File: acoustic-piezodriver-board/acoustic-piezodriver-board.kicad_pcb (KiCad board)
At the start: 4 copper layers, 86 x 90 mm, 129 parts, among them J301 Conn_02x06_Odd_Even, J501 Conn_02x06_Odd_Even, P201 WJ128V-5.0-3P, P301 WJ128V-5.0-3P, Q501 AO3400A, Q502 AO3400A, U10 NCE6005AS, U201 UCC27282DR, U202 UCC27282DR, U401 AMS1117-3.3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

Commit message: finished schematic, routing
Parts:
- removed P301: WJ128V-5.0-3P, iw-connector:WJ128V-5.0-3P
- removed U401: AMS1117-3.3, Package_TO_SOT_SMD:SOT-223-3_TabPin2
- added C101: 22uF, Capacitor_SMD:C_0805_2012Metric, F.Cu at (-48.2, 146.8)
- added C102: 0.1uF, Capacitor_SMD:C_0402_1005Metric, F.Cu at (-42.0, 128.7)
- added C103: 1nF, Capacitor_SMD:C_0402_1005Metric, F.Cu at (-42.0, 130.7)
- added C210: 0.1uF, Capacitor_SMD:C_0402_1005Metric, F.Cu at (-37.1, 134.7)
- added C211: 1nF, Capacitor_SMD:C_0402_1005Metric, F.Cu at (-37.1, 136.7)
- added C301: 0.1uF, Capacitor_SMD:C_0201_0603Metric, F.Cu at (-38.9, 159.2)
- added C304: 0.1uF, Capacitor_SMD:C_0402_1005Metric, F.Cu at (-38.7, 157.3)
- added C404: 0.1uF, Capacitor_SMD:C_0402_1005Metric, F.Cu at (-51.9, 153.3)
- added C405: 220nF, Capacitor_SMD:C_0402_1005Metric, F.Cu at (-51.9, 155.2)
- added C406: 220nF, Capacitor_SMD:C_0402_1005Metric, F.Cu at (-51.9, 157.2)
- added C523: 0.1uF, Capacitor_SMD:C_0402_1005Metric, F.Cu at (-33.1, 140.7)
- added C524: 0.1uF, Capacitor_SMD:C_0402_1005Metric, F.Cu at (-33.1, 142.6)
- added L301: 100uH, iw-inductor:PSPMAA1050H-101M-ANP, F.Cu at (108.2, 120.4)
- added L501: 100uH, iw-inductor:PSPMAA1050H-101M-ANP, F.Cu at (-48.1, 178.0)
- added L502: 100uH, iw-inductor:PSPMAA1050H-101M-ANP, F.Cu at (-48.1, 189.3)
- added P101: WJ128V-5.0-3P, iw-connector:WJ128V-5.0-3P, F.Cu at (-51.6, 133.3)
- added R406: 0, Resistor_SMD:R_0603_1608Metric_Pad0.98x0.95mm_HandSolder, F.Cu at (-48.3, 154.1)
- added R407: 10k, Resistor_SMD:R_0603_1608Metric, F.Cu at (-58.3, 151.6)
- added R408: 10k, Resistor_SMD:R_0603_1608Metric, F.Cu at (-58.3, 154.1)
- added R409: 1k, Resistor_SMD:R_0402_1005Metric, F.Cu at (-54.8, 151.3)
- added R410: 1k, Resistor_SMD:R_0402_1005Metric, F.Cu at (-54.8, 153.3)
- added R411: 10k, Resistor_SMD:R_0603_1608Metric, F.Cu at (-58.3, 156.6)
- added R412: 1k8, Resistor_SMD:R_0603_1608Metric, F.Cu at (-58.3, 159.1)
- added R413: 20k, Resistor_SMD:R_0402_1005Metric, F.Cu at (-54.8, 155.3)
- added R414: 1k, Resistor_SMD:R_0402_1005Metric, F.Cu at (-54.8, 157.3)
- added TP301: TestPoint_Flag, TestPoint:TestPoint_THTPad_D2.0mm_Drill1.0mm, F.Cu at (-42.1, 158.4)
- added TP501: TestPoint_Flag, TestPoint:TestPoint_THTPad_D2.0mm_Drill1.0mm, F.Cu at (-36.6, 141.7)
- added TP502: TestPoint_Flag, TestPoint:TestPoint_THTPad_D2.0mm_Drill1.0mm, F.Cu at (-36.6, 145.8)
- added U101: AMS1117-3.3, Package_TO_SOT_SMD:SOT-223-3_TabPin2, F.Cu at (-55.4, 143.5)
- added U102: TMCS1108A3UQDR, iw-power:TMCS1108A3UQDR, F.Cu at (-45.6, 142.3)
- added U204: TMCS1108A3UQDR, iw-power:TMCS1108A3UQDR, F.Cu at (-33.7, 130.7)
- added U302: TMCS1108A3UQDR, iw-power:TMCS1108A3UQDR, F.Cu at (-39.3, 153.3)
- added U404: ADS1115IDGS, Package_SO:TSSOP-10_3x3mm_P0.5mm, F.Cu at (-49.9, 160.5)
- C402: value 22uF -> 220nF; footprint Capacitor_SMD:C_0805_2012Metric -> Capacitor_SMD:C_0402_1005Metric
- L4: footprint iw-inductor:PSPMAC1045H-101M-ANP -> iw-inductor:PSPMAA1050H-101M-ANP
- R402: value 4.7k -> 0; footprint Resistor_SMD:R_0402_1005Metric -> Resistor_SMD:R_0603_1608Metric_Pad0.98x0.95mm_HandSolder
- moved R402 73.2 mm to (-48.3, 151.6)
- moved C402 64.7 mm to (-51.9, 151.3)
- moved C8 21.0 mm to (65.1, 90.2)
- moved R5 21.0 mm to (65.2, 96.4)
- moved C2 21.0 mm to (51.1, 117.2)
- moved C3 21.0 mm to (48.9, 83.0)
- moved C4 21.0 mm to (38.9, 112.5)
- moved C9 21.0 mm to (44.8, 105.0)
- moved D11 21.0 mm to (54.6, 113.9)
- moved D9 21.0 mm to (45.8, 111.2)
- moved R1 21.0 mm to (51.7, 113.9)
- moved R2 21.0 mm to (62.7, 111.1)
- moved R4 21.0 mm to (42.9, 111.0)
- moved U201 21.0 mm to (60.2, 116.2)
- moved U202 21.0 mm to (40.2, 116.3)
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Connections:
- C3 pad 1: /INVERTER/VDC -> /INVERTER/VINV_N
- C4 pad 1: /INVERTER/VDC -> /INVERTER/VINV_N
- C40 pad 1: /COMPUTE_POWER/6V -> +6V
- C402 pad 1: +3V3 -> Net-(U404-AIN1)
- C41 pad 1: /COMPUTE_POWER/6V -> +6V
- C42 pad 1: /COMPUTE_POWER/6V -> +6V
- C43 pad 1: /COMPUTE_POWER/6V -> +6V
- C516 pad 1: /INVERTER/VDC -> /INVERTER/VINV_P
- C517 pad 1: /INVERTER/VDC -> /INVERTER/VINV_P
- C518 pad 1: /INVERTER/VDC -> /INVERTER/VINV_P
- C519 pad 1: /INVERTER/VDC -> /INVERTER/VINV_P
- D2 pad 1: /COMPUTE_POWER/6V -> +6V
- D501 pad 1: /INVERTER/VDC -> /INVERTER/VINV_P
- D504 pad 1: /INVERTER/VDC -> /INVERTER/VINV_P
- J301 pad 10: /COMPUTE_POWER/6V -> /COMPUTE_POWER/6V_N
- J301 pad 12: /COMPUTE_POWER/6V -> /COMPUTE_POWER/6V_N
- J301 pad 2: /COMPUTE_POWER/6V -> /COMPUTE_POWER/6V_N
- J301 pad 4: /COMPUTE_POWER/6V -> /COMPUTE_POWER/6V_N
- J301 pad 6: /COMPUTE_POWER/6V -> /COMPUTE_POWER/6V_N
- J301 pad 8: /COMPUTE_POWER/6V -> /COMPUTE_POWER/6V_N
- J501 pad 5: unconnected-(J501-Pin_5-Pad5) -> /SENSORS_CONN/ADC_ALERT
- R10 pad 2: /INVERTER/VDC -> /INVERTER/VINV_N
- R23 pad 1: /COMPUTE_POWER/6V -> +6V
- R512 pad 1: /INVERTER/VDC -> /INVERTER/VINV_P
- R7 pad 2: /INVERTER/VDC -> /INVERTER/VINV_N
- U201 pad 1: /INVERTER/VDC -> /INVERTER/VINV_N
- U202 pad 1: /INVERTER/VDC -> /INVERTER/VINV_N
- U403 pad 4: GND -> Net-(U403-ADD0)
- U6 pad 7: /INVERTER/VDC -> /INVERTER/VINV_N
- U6 pad 8: /INVERTER/VDC -> /INVERTER/VINV_N
- U7 pad 7: /INVERTER/VDC -> /INVERTER/VINV_N
- U7 pad 8: /INVERTER/VDC -> /INVERTER/VINV_N

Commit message: replaced dual 10uH inductors with single 22uH higher VDC resistant one, started laying out 40 V boost
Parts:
- removed C103, C211: 1nF, Capacitor_SMD:C_0402_1005Metric
- removed L4: 100uH, iw-inductor:PSPMAA1050H-101M-ANP
- removed TP301: TestPoint_Flag, TestPoint:TestPoint_THTPad_D2.0mm_Drill1.0mm
- added L302: 100uH, iw-inductor:PSPMAA1050H-101M-ANP, F.Cu at (123.0, 124.5)
- added L505: 22uH, iw-inductor:PA4343.223NLT, F.Cu at (69.3, 61.5)
- moved C501 207.7 mm to (75.9, 162.5)
- moved C503 207.7 mm to (58.3, 162.4)
- moved C505 207.7 mm to (58.3, 165.4)
- moved C506 207.7 mm to (58.3, 168.4)
- moved C507 207.7 mm to (58.3, 171.4)
- moved C508 207.7 mm to (58.3, 174.4)
- moved C510 207.7 mm to (80.2, 161.8)
- moved C511 207.7 mm to (80.2, 163.8)
- moved D503 207.7 mm to (69.1, 167.7)
- moved U502 207.7 mm to (76.8, 173.3)
- moved R505 203.0 mm to (91.8, 174.0)
- moved Q501 200.6 mm to (78.3, 177.3)
- moved U501 200.6 mm to (69.5, 178.0)
- moved C512 200.2 mm to (53.9, 178.2)
- moved R506 200.2 mm to (57.9, 178.2)
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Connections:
- U102 pad 6: unconnected-(U102-NC-Pad6) -> GND
- U201 pad 9: (no net) -> GND
- U202 pad 9: (no net) -> GND
- U204 pad 6: unconnected-(U204-NC-Pad6) -> GND
- U302 pad 6: unconnected-(U302-NC-Pad6) -> GND

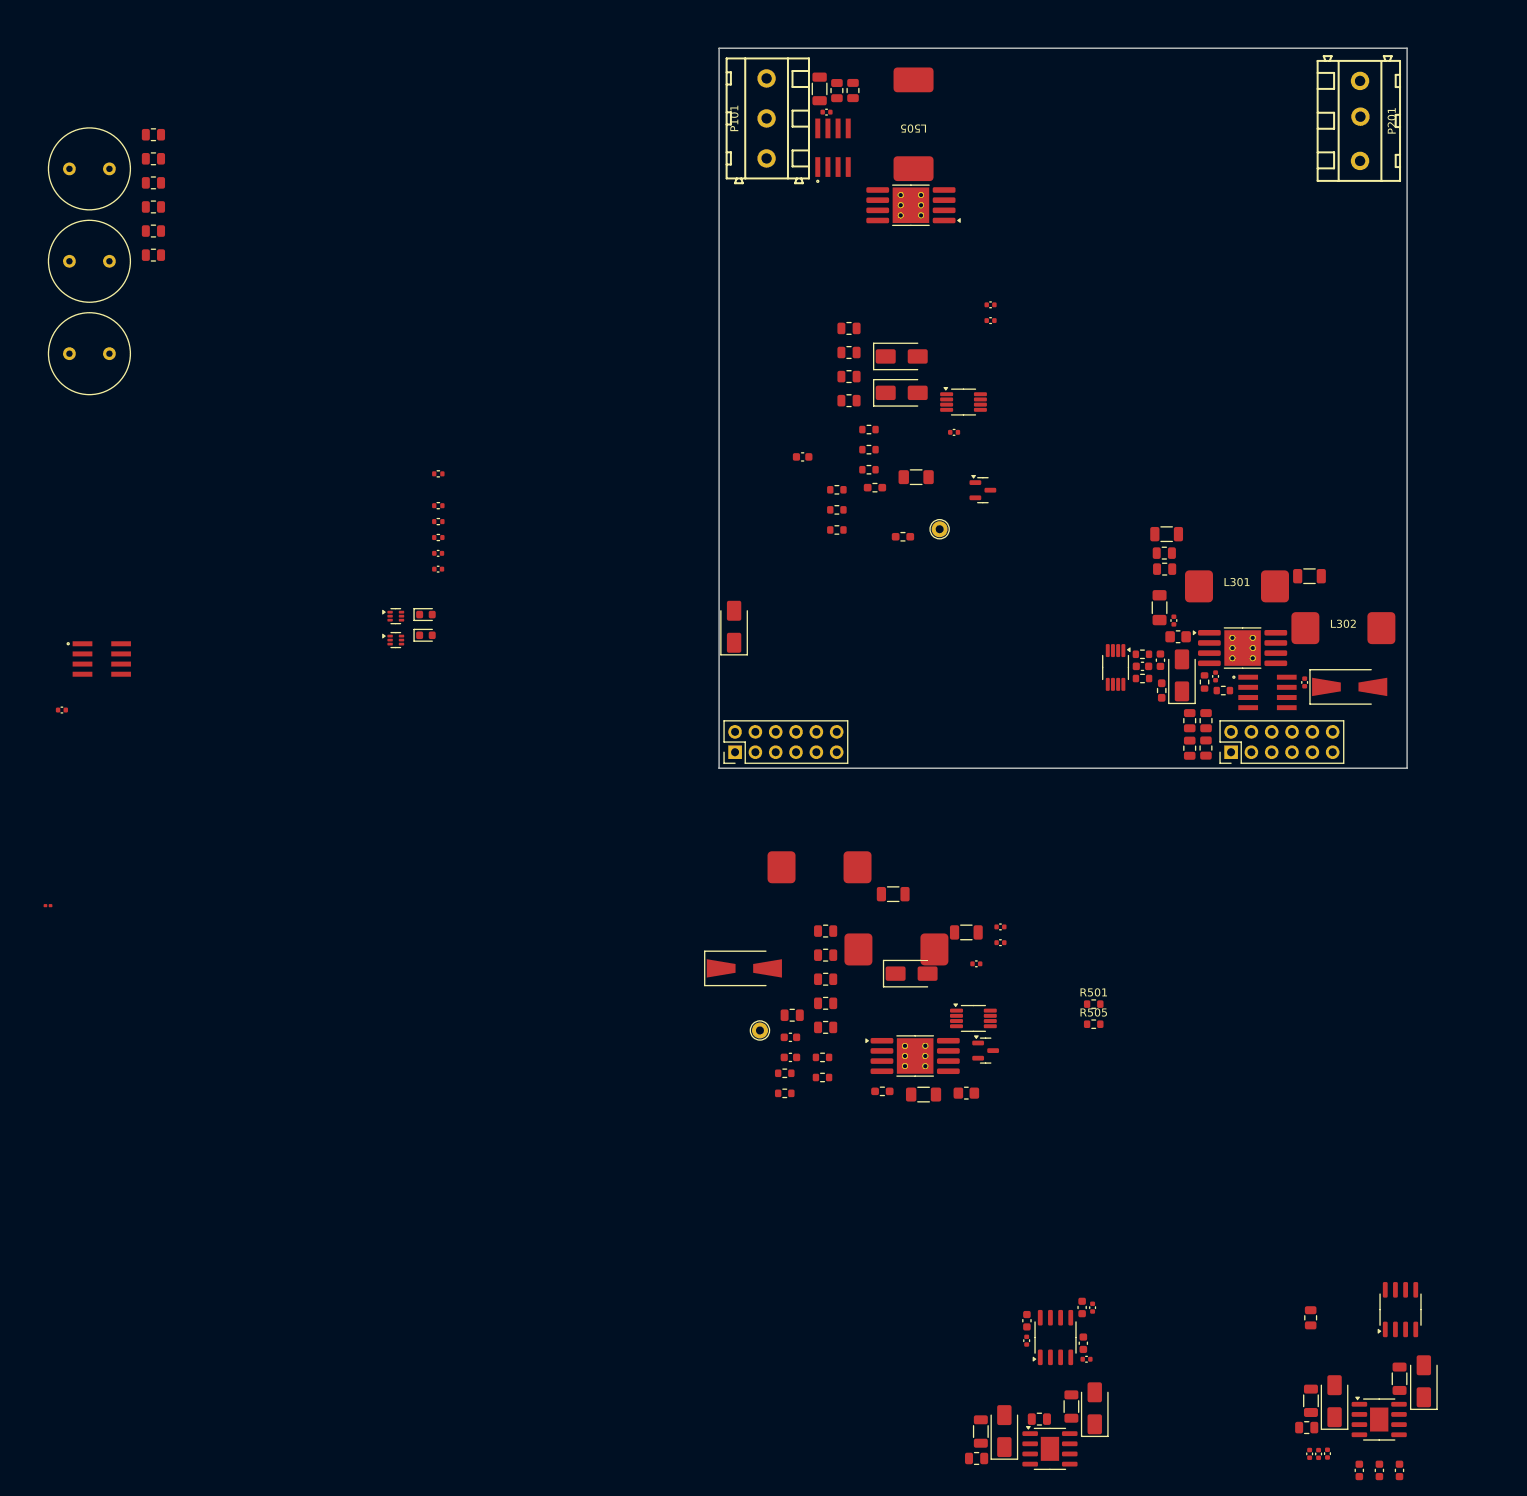
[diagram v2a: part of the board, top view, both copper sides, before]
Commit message: placed inverter and 40 V boost (next) place 10 V SEPIC driver
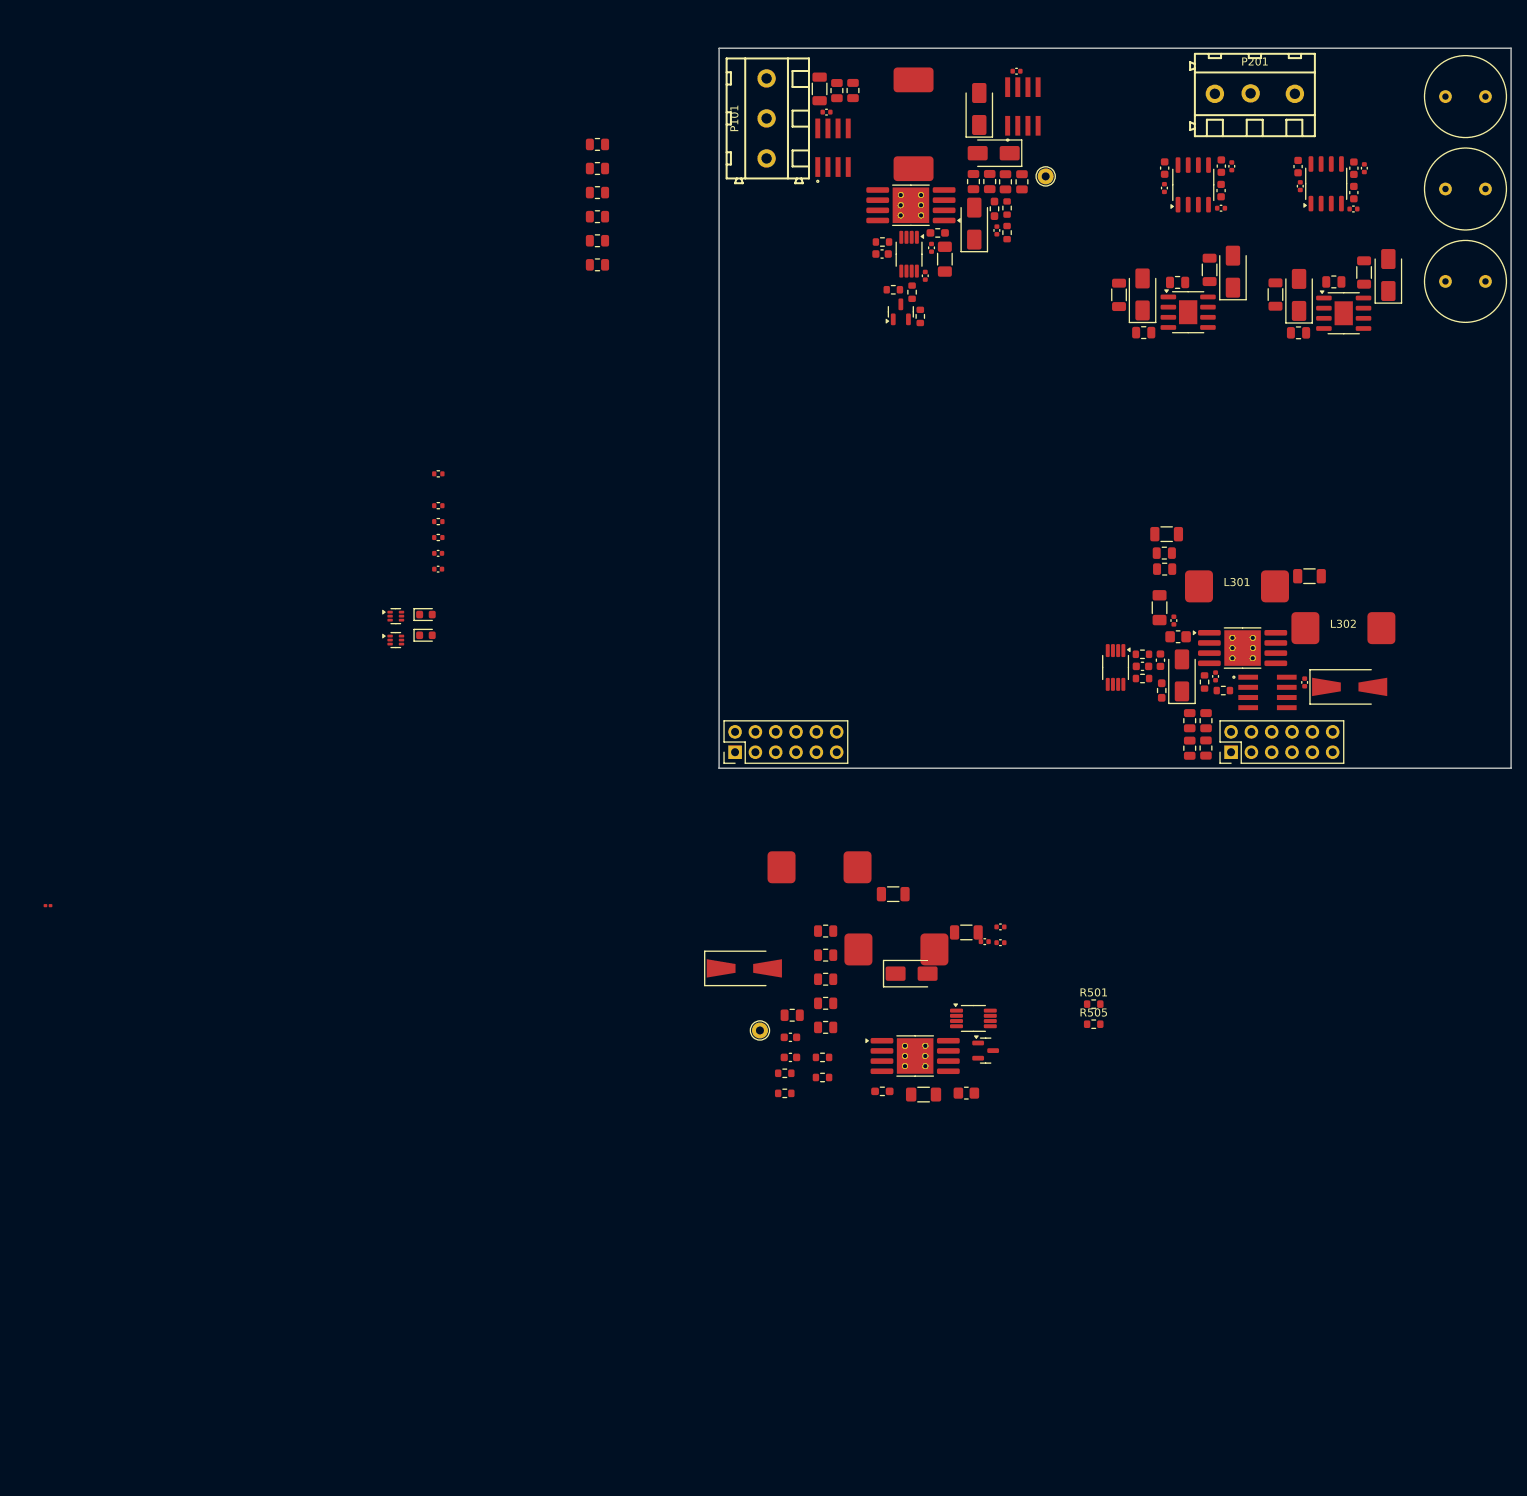
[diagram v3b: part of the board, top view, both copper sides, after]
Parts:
- moved C201 172.2 mm to (135.8, 58.0)
- moved C202 172.2 mm to (135.8, 69.6)
- moved C203 172.2 mm to (135.8, 81.2)
- moved R10 163.2 mm to (117.4, 66.8), turned to 90 degrees
- moved R9 162.8 mm to (124.3, 67.0), turned to 90 degrees
- moved C6 160.7 mm to (125.7, 67.0)
- moved R8 159.8 mm to (124.3, 70.0), turned to 90 degrees
- moved C12 158.5 mm to (117.7, 69.2), turned to 90 degrees
- moved C11 155.7 mm to (124.3, 72.1), turned to 180 degrees
- moved C10 145.1 mm to (100.7, 69.5)
- moved R6 145.1 mm to (107.8, 69.8)
- moved R7 145.1 mm to (100.7, 67.0)
- moved U7 145.1 mm to (104.3, 69.1)
- moved C9 144.9 mm to (107.7, 72.0)
- moved C8 143.7 mm to (109.1, 66.8)
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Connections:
- C201 pad 1: /INVERTER/10V -> /INVERTER/VINV_N
- C202 pad 1: /INVERTER/10V -> /INVERTER/VINV_N
- C203 pad 1: /INVERTER/10V -> /INVERTER/VINV_N
- C204 pad 2: /INVERTER/10V -> /INVERTER/VINV_N
- C205 pad 2: /INVERTER/10V -> /INVERTER/VINV_N
- C206 pad 2: /INVERTER/10V -> /INVERTER/VINV_N
- C207 pad 2: /INVERTER/10V -> /INVERTER/VINV_N
- C208 pad 2: /INVERTER/10V -> /INVERTER/VINV_N
- C209 pad 2: /INVERTER/10V -> /INVERTER/VINV_N
- C3 pad 1: /INVERTER/VINV_N -> /INVERTER/10V
- C4 pad 1: /INVERTER/VINV_N -> /INVERTER/10V
- U201 pad 1: /INVERTER/VINV_N -> /INVERTER/10V
- U202 pad 1: /INVERTER/VINV_N -> /INVERTER/10V
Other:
- board size 86 x 90 mm -> 99 x 90 mm
